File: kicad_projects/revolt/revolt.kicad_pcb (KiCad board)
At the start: 2 copper layers, 144.9 x 111.9 mm, 85 parts, among them J1 IDC-Header_2x07_P2.54mm_Verti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

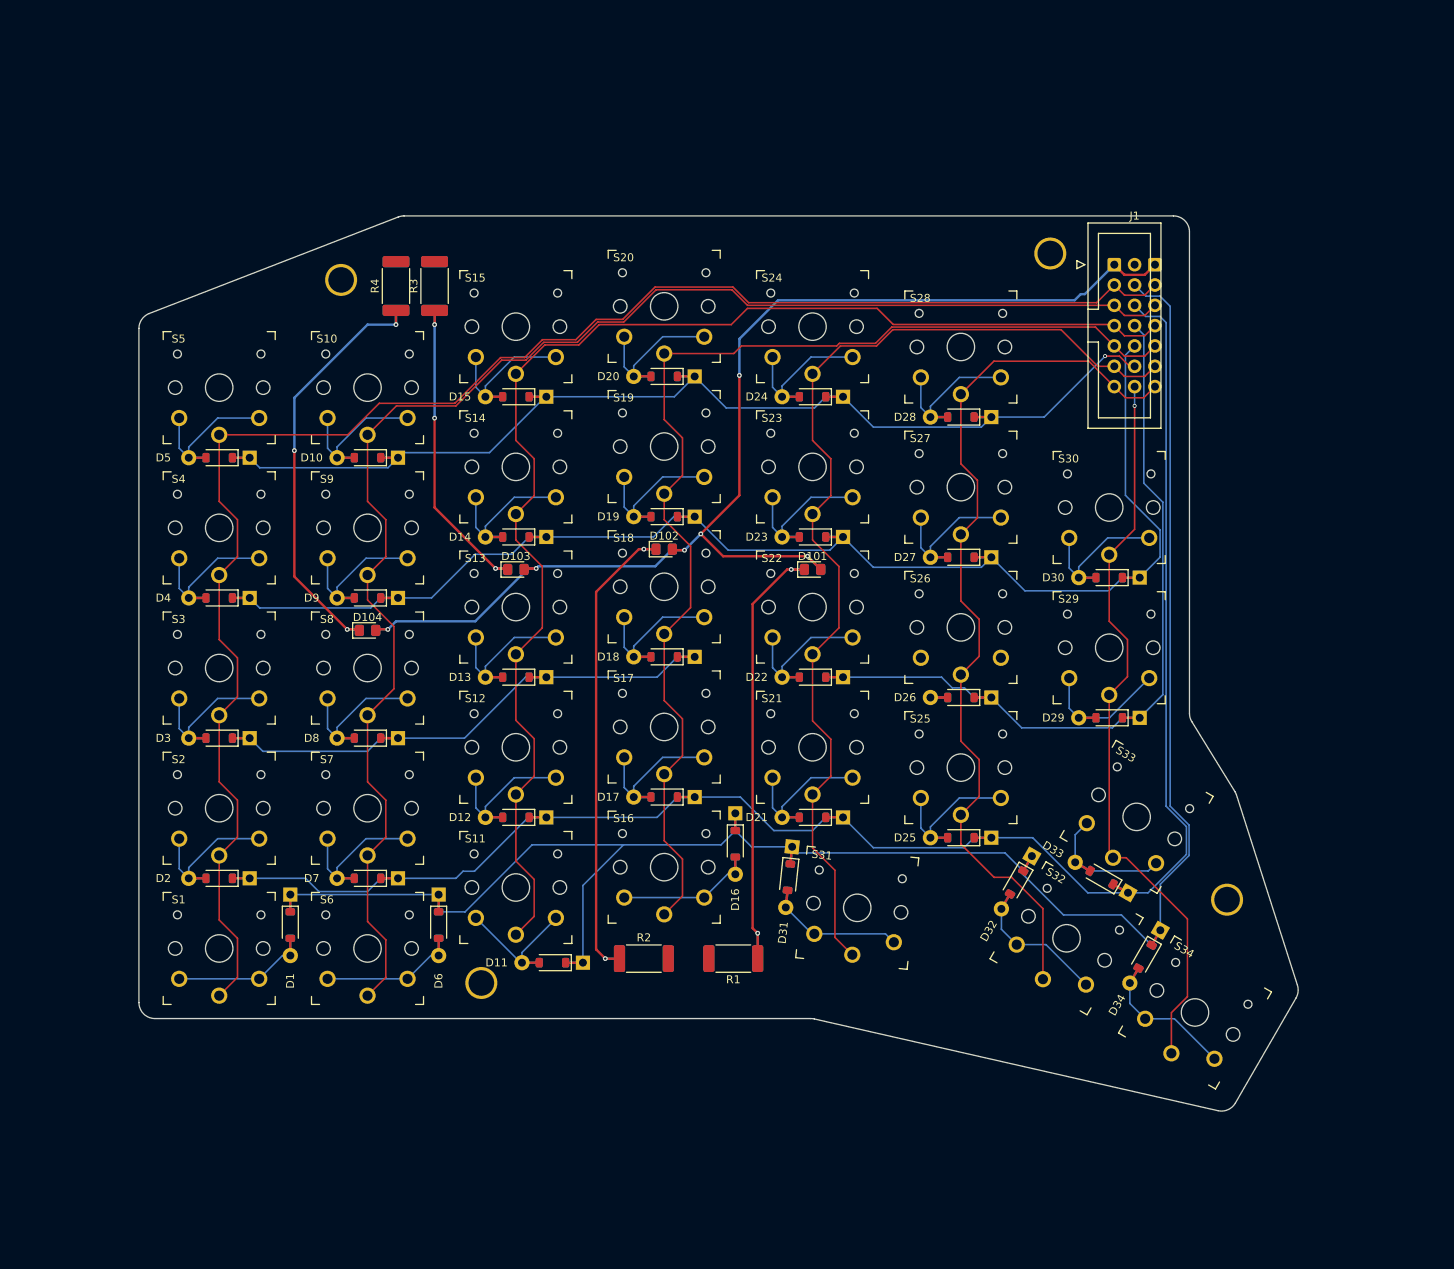
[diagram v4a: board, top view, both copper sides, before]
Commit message: Ground plane and stitching
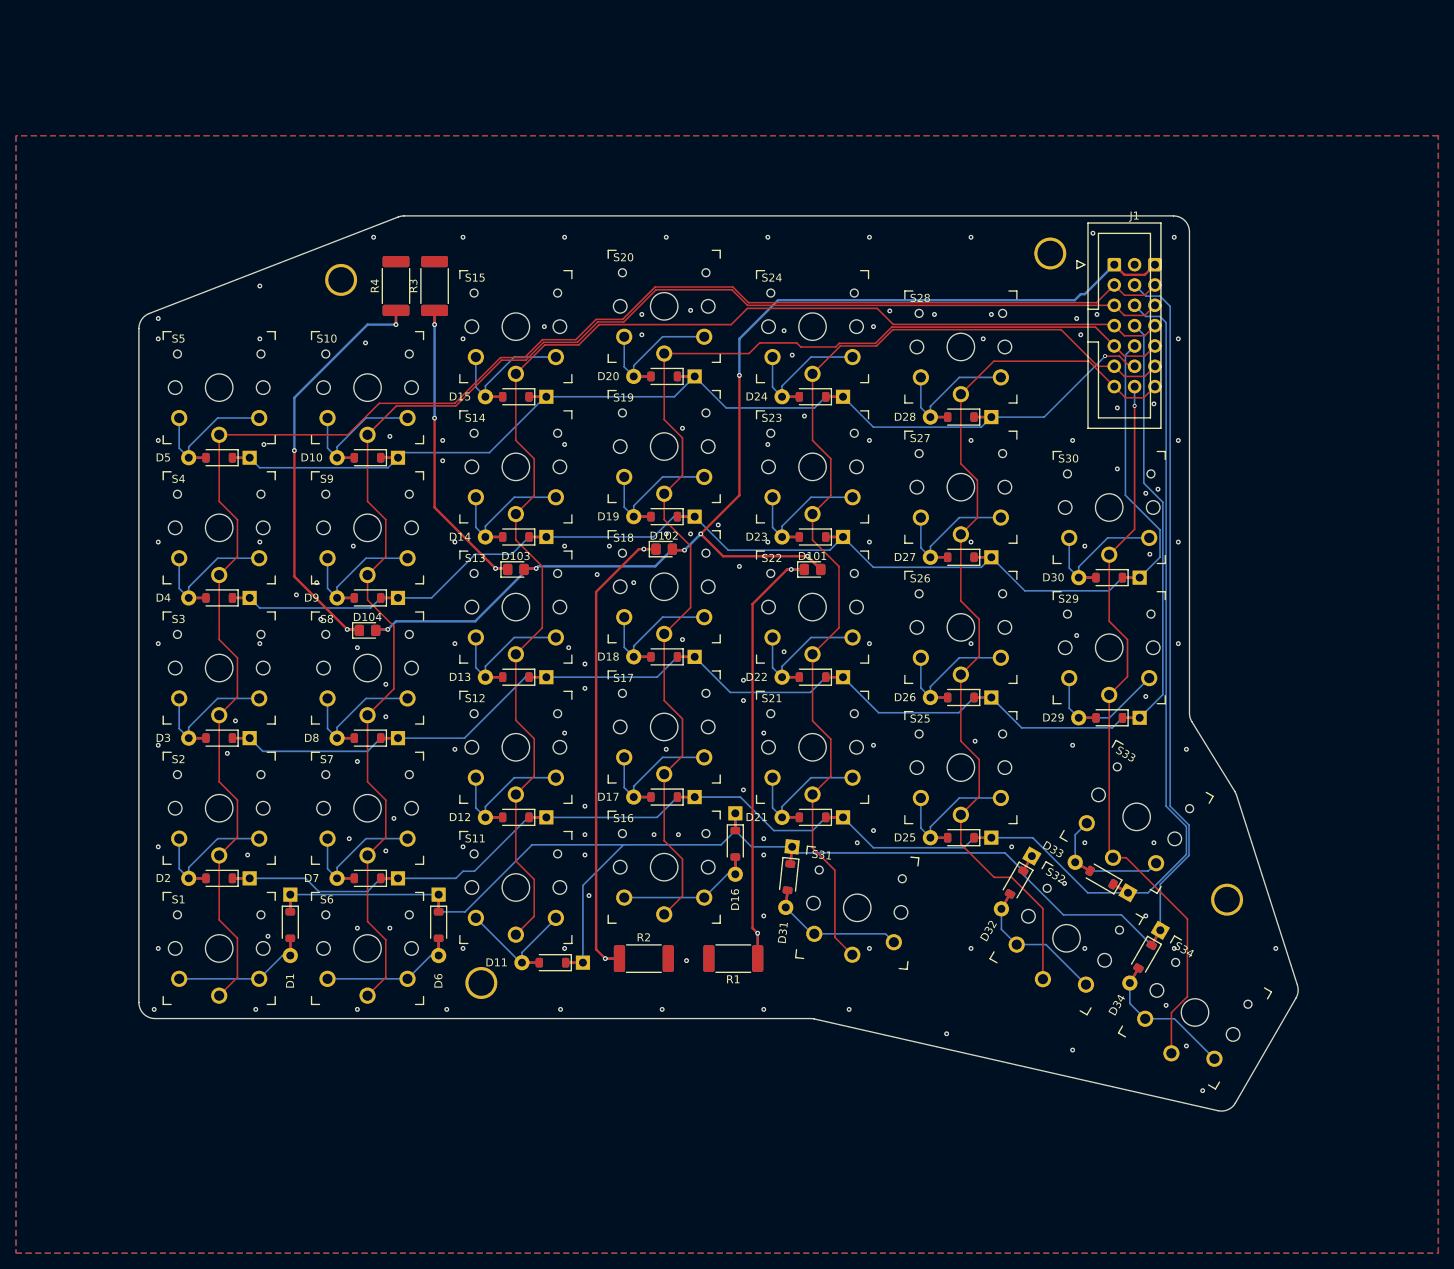
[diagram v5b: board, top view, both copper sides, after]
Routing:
- net /ROW2: track 142.3 -> 162.9 mm
- net Net-(D26-A): track 0.00 -> 17.1 mm
- net GND: vias 0 -> 147
- added copper zone on B.Cu, net GND
- added copper zone on F.Cu, net GND

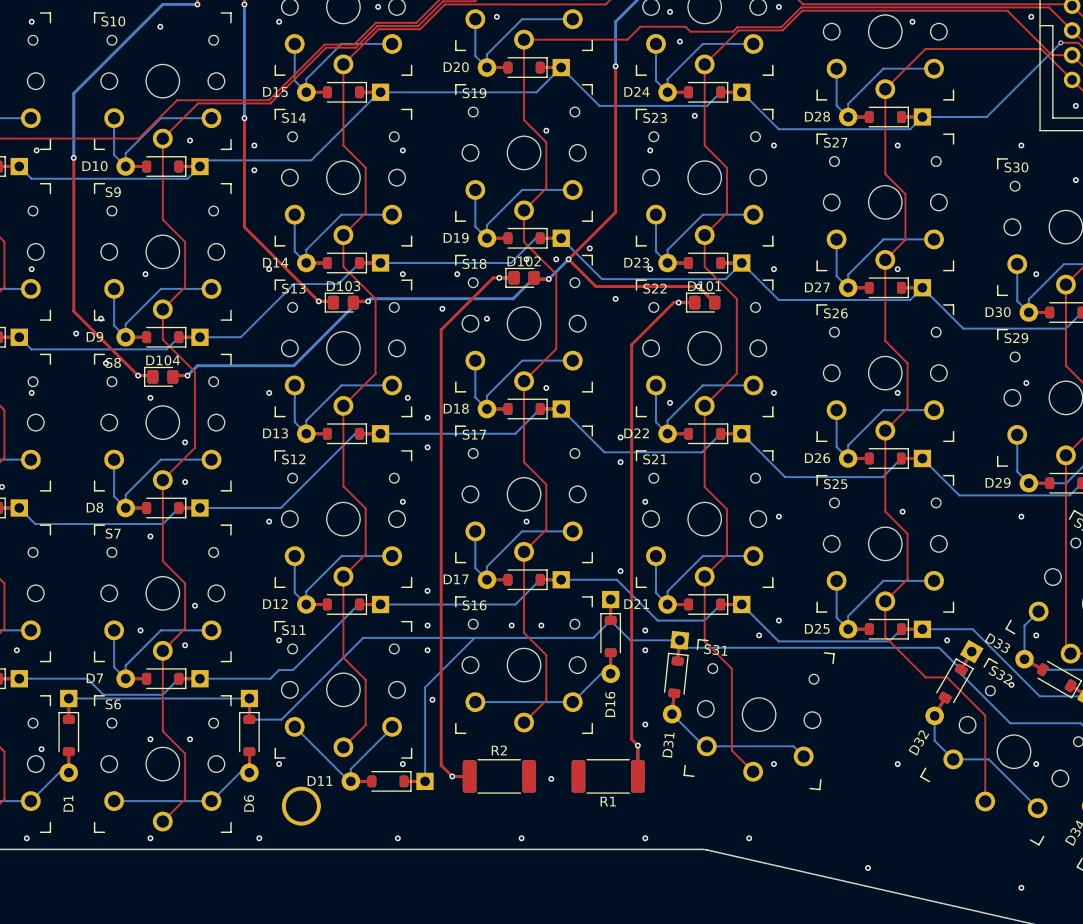
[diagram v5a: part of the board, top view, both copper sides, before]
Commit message: Add the url on the silkscreen, more stitching
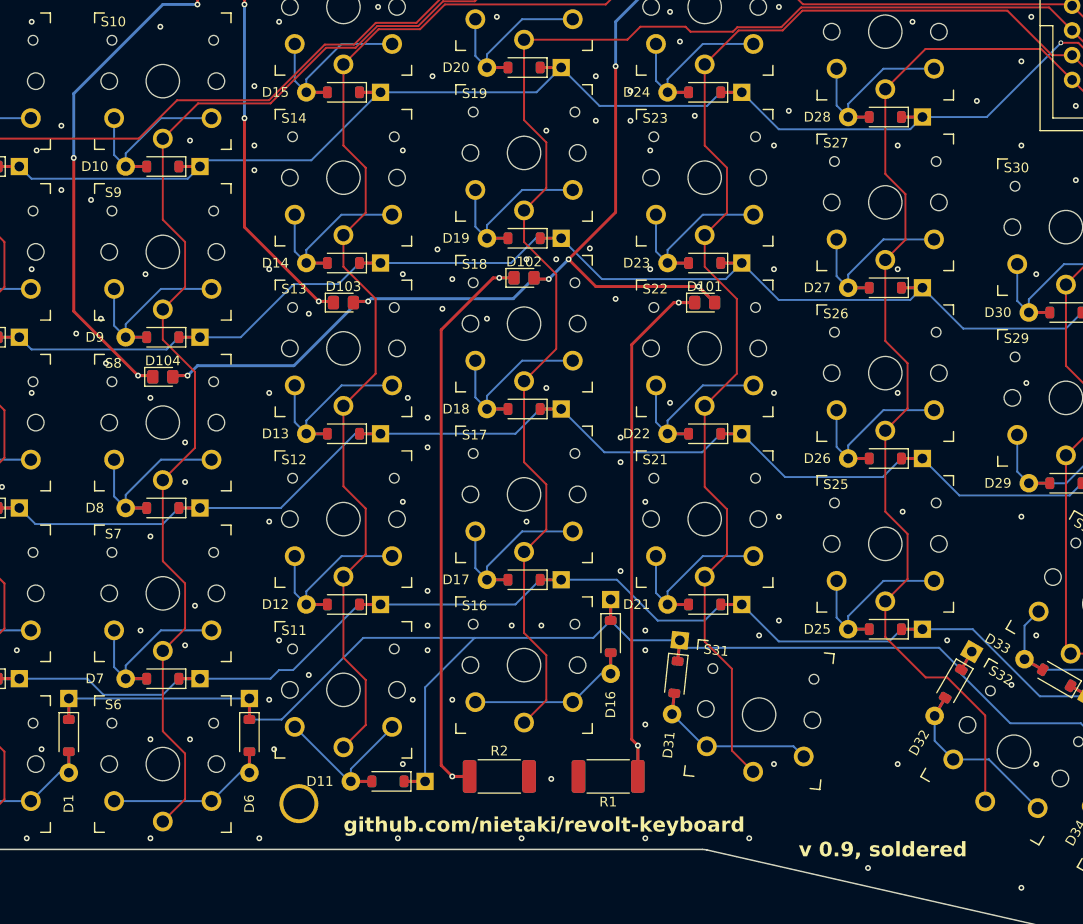
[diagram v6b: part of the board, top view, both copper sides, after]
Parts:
- moved H4 0.36 mm to (134.1, 156.5)
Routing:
- net GND: vias 147 -> 164
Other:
- board text added: "github.com/nietaki/revolt-keyboard"
- board text added: "v 0.9, soldered"
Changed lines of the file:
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@@
   )
   (footprint "revolt_footprints:HOLE_M3" (layer "F.Cu")
-    (at 134.366 156.718)
+    (at 134.112 156.464)
     (property "Sheetfile" "revolt.kicad_sch")
     (property "Sheetname" "")
@@
   (gr_line (start 228.765614 133.230142) (end 236.376007 156.985216)
     (stroke (width 0.15) (type solid)) (layer "Edge.Cuts"))
+  (gr_text "v 0.9, soldered" (at 185.42 162.052) (layer "F.SilkS")
+    (effects (font (size 1.5 1.5) (thickness 0.3) bold) (justify left bottom))
+  )
+  (gr_text "github.com/nietaki/revolt-keyboard" (at 138.684 159.512) (layer "F.SilkS")
+    (effects (font (size 1.5 1.5) (thickness 0.3) bold) (justify left bottom))
+  )
   (segment (start 220.472 72.136) (end 220.472 134.62) (width 0.2) (layer "B.Cu") (net 1))
   (segment (start 216.027 69.469) (end 217.417 70.859) (width 0.2) (layer "B.Cu") (net 1))
@@
   (via (at 93.98 76.2) (size 0.6) (drill 0.3) (layers "F.Cu" "B.Cu") (free) (net 48))
   (via (at 107.696 150.876) (size 0.6) (drill 0.3) (layers "F.Cu" "B.Cu") (free) (net 48))
-  (via (at 147.828 145.796) (size 0.6) (drill 0.3) (layers "F.Cu" "B.Cu") (free) (net 48))
+  (via (at 145.796 145.796) (size 0.6) (drill 0.3) (layers "F.Cu" "B.Cu") (free) (net 48))
   (via (at 103.632 123.952) (size 0.6) (drill 0.3) (layers "F.Cu" "B.Cu") (free) (net 48))
   (via (at 93.98 114.3) (size 0.6) (drill 0.3) (layers "F.Cu" "B.Cu") (free) (net 48))
   (via (at 221.488 114.3) (size 0.6) (drill 0.3) (layers "F.Cu" "B.Cu") (free) (net 48))
   (via (at 118.364 102.108) (size 0.6) (drill 0.3) (layers "F.Cu" "B.Cu") (free) (net 48))
+  (via (at 109.728 93.472) (size 0.6) (drill 0.3) (layers "F.Cu" "B.Cu") (free) (net 48))
   (via (at 183.388 74.676) (size 0.6) (drill 0.3) (layers "F.Cu" "B.Cu") (free) (net 48))
   (via (at 129.54 88.9) (size 0.6) (drill 0.3) (layers "F.Cu" "B.Cu") (free) (net 48))
@@
   (via (at 182.88 114.3) (size 0.6) (drill 0.3) (layers "F.Cu" "B.Cu") (free) (net 48))
   (via (at 220.98 63.5) (size 0.6) (drill 0.3) (layers "F.Cu" "B.Cu") (free) (net 48))
+  (via (at 203.708 84.328) (size 0.6) (drill 0.3) (layers "F.Cu" "B.Cu") (free) (net 48))
   (via (at 218.948 94.996) (size 0.6) (drill 0.3) (layers "F.Cu" "B.Cu") (free) (net 48))
   (via (at 207.264 144.272) (size 0.6) (drill 0.3) (layers "F.Cu" "B.Cu") (free) (net 48))
   (via (at 113.792 106.68) (size 0.6) (drill 0.3) (layers "F.Cu" "B.Cu") (free) (net 48))
-  (via (at 150.368 102.108) (size 0.6) (drill 0.3) (layers "F.Cu" "B.Cu") (free) (net 48))
+  (via (at 149.86 102.616) (size 0.6) (drill 0.3) (layers "F.Cu" "B.Cu") (free) (net 48))
   (via (at 118.872 160.02) (size 0.6) (drill 0.3) (layers "F.Cu" "B.Cu") (free) (net 48))
   (via (at 219.964 159.512) (size 0.6) (drill 0.3) (layers "F.Cu" "B.Cu") (free) (net 48))
+  (via (at 149.86 145.796) (size 0.6) (drill 0.3) (layers "F.Cu" "B.Cu") (free) (net 48))
   (via (at 154.432 73.152) (size 0.6) (drill 0.3) (layers "F.Cu" "B.Cu") (free) (net 48))
   (via (at 196.088 126.492) (size 0.6) (drill 0.3) (layers "F.Cu" "B.Cu") (free) (net 48))
@@
   (via (at 114.3 111.252) (size 0.6) (drill 0.3) (layers "F.Cu" "B.Cu") (free) (net 48))
   (via (at 169.672 160.02) (size 0.6) (drill 0.3) (layers "F.Cu" "B.Cu") (free) (net 48))
-  (via (at 132.08 152.4) (size 0.6) (drill 0.3) (layers "F.Cu" "B.Cu") (free) (net 48))
+  (via (at 131.572 150.876) (size 0.6) (drill 0.3) (layers "F.Cu" "B.Cu") (free) (net 48))
+  (via (at 164.592 81.788) (size 0.6) (drill 0.3) (layers "F.Cu" "B.Cu") (free) (net 48))
   (via (at 106.68 69.596) (size 0.6) (drill 0.3) (layers "F.Cu" "B.Cu") (free) (net 48))
+  (via (at 129.54 82.804) (size 0.6) (drill 0.3) (layers "F.Cu" "B.Cu") (free) (net 48))
   (via (at 172.212 75.184) (size 0.6) (drill 0.3) (layers "F.Cu" "B.Cu") (free) (net 48))
+  (via (at 184.404 85.344) (size 0.6) (drill 0.3) (layers "F.Cu" "B.Cu") (free) (net 48))
   (via (at 93.472 160.02) (size 0.6) (drill 0.3) (layers "F.Cu" "B.Cu") (free) (net 48))
+  (via (at 135.128 143.256) (size 0.6) (drill 0.3) (layers "F.Cu" "B.Cu") (free) (net 48))
   (via (at 131.064 101.6) (size 0.6) (drill 0.3) (layers "F.Cu" "B.Cu") (free) (net 48))
   (via (at 93.98 152.4) (size 0.6) (drill 0.3) (layers "F.Cu" "B.Cu") (free) (net 48))
@@
   (via (at 144.78 152.4) (size 0.6) (drill 0.3) (layers "F.Cu" "B.Cu") (free) (net 48))
   (via (at 157.48 63.5) (size 0.6) (drill 0.3) (layers "F.Cu" "B.Cu") (free) (net 48))
+  (via (at 148.336 99.568) (size 0.6) (drill 0.3) (layers "F.Cu" "B.Cu") (free) (net 48))
   (via (at 208.788 113.284) (size 0.6) (drill 0.3) (layers "F.Cu" "B.Cu") (free) (net 48))
+  (via (at 112.776 94.488) (size 0.6) (drill 0.3) (layers "F.Cu" "B.Cu") (free) (net 48))
   (via (at 153.416 106.68) (size 0.6) (drill 0.3) (layers "F.Cu" "B.Cu") (free) (net 48))
   (via (at 160.528 100.584) (size 0.6) (drill 0.3) (layers "F.Cu" "B.Cu") (free) (net 48))
@@
   (via (at 167.132 132.588) (size 0.6) (drill 0.3) (layers "F.Cu" "B.Cu") (free) (net 48))
   (via (at 208.788 73.66) (size 0.6) (drill 0.3) (layers "F.Cu" "B.Cu") (free) (net 48))
+  (via (at 135.128 106.172) (size 0.6) (drill 0.3) (layers "F.Cu" "B.Cu") (free) (net 48))
   (via (at 221.488 76.2) (size 0.6) (drill 0.3) (layers "F.Cu" "B.Cu") (free) (net 48))
   (via (at 122.936 88.392) (size 0.6) (drill 0.3) (layers "F.Cu" "B.Cu") (free) (net 48))
@@
   (via (at 208.28 165.1) (size 0.6) (drill 0.3) (layers "F.Cu" "B.Cu") (free) (net 48))
   (via (at 93.98 101.6) (size 0.6) (drill 0.3) (layers "F.Cu" "B.Cu") (free) (net 48))
+  (via (at 164.592 86.36) (size 0.6) (drill 0.3) (layers "F.Cu" "B.Cu") (free) (net 48))
   (via (at 182.88 152.4) (size 0.6) (drill 0.3) (layers "F.Cu" "B.Cu") (free) (net 48))
   (via (at 144.78 102.108) (size 0.6) (drill 0.3) (layers "F.Cu" "B.Cu") (free) (net 48))
@@
   (via (at 198.12 73.152) (size 0.6) (drill 0.3) (layers "F.Cu" "B.Cu") (free) (net 48))
   (via (at 195.58 88.9) (size 0.6) (drill 0.3) (layers "F.Cu" "B.Cu") (free) (net 48))
+  (via (at 131.064 145.796) (size 0.6) (drill 0.3) (layers "F.Cu" "B.Cu") (free) (net 48))
   (via (at 180.34 160.02) (size 0.6) (drill 0.3) (layers "F.Cu" "B.Cu") (free) (net 48))
   (via (at 118.872 149.86) (size 0.6) (drill 0.3) (layers "F.Cu" "B.Cu") (free) (net 48))
@@
   (via (at 191.008 73.152) (size 0.6) (drill 0.3) (layers "F.Cu" "B.Cu") (free) (net 48))
   (via (at 102.616 128.016) (size 0.6) (drill 0.3) (layers "F.Cu" "B.Cu") (free) (net 48))
+  (via (at 208.28 80.264) (size 0.6) (drill 0.3) (layers "F.Cu" "B.Cu") (free) (net 48))
   (via (at 173.228 78.232) (size 0.6) (drill 0.3) (layers "F.Cu" "B.Cu") (free) (net 48))
   (via (at 208.28 88.9) (size 0.6) (drill 0.3) (layers "F.Cu" "B.Cu") (free) (net 48))
@@
   (via (at 132.08 63.5) (size 0.6) (drill 0.3) (layers "F.Cu" "B.Cu") (free) (net 48))
   (via (at 130.048 160.02) (size 0.6) (drill 0.3) (layers "F.Cu" "B.Cu") (free) (net 48))
+  (via (at 168.148 86.36) (size 0.6) (drill 0.3) (layers "F.Cu" "B.Cu") (free) (net 48))
+  (via (at 147.828 81.788) (size 0.6) (drill 0.3) (layers "F.Cu" "B.Cu") (free) (net 48))
   (via (at 211.328 73.152) (size 0.6) (drill 0.3) (layers "F.Cu" "B.Cu") (free) (net 48))
   (via (at 93.98 88.9) (size 0.6) (drill 0.3) (layers "F.Cu" "B.Cu") (free) (net 48))
   (via (at 144.272 160.02) (size 0.6) (drill 0.3) (layers "F.Cu" "B.Cu") (free) (net 48))
+  (via (at 109.728 86.868) (size 0.6) (drill 0.3) (layers "F.Cu" "B.Cu") (free) (net 48))
   (via (at 154.432 75.692) (size 0.6) (drill 0.3) (layers "F.Cu" "B.Cu") (free) (net 48))
   (via (at 167.132 121.412) (size 0.6) (drill 0.3) (layers "F.Cu" "B.Cu") (free) (net 48))
   (via (at 117.856 138.684) (size 0.6) (drill 0.3) (layers "F.Cu" "B.Cu") (free) (net 48))
   (via (at 182.88 63.5) (size 0.6) (drill 0.3) (layers "F.Cu" "B.Cu") (free) (net 48))
+  (via (at 168.148 83.312) (size 0.6) (drill 0.3) (layers "F.Cu" "B.Cu") (free) (net 48))
   (via (at 106.68 101.6) (size 0.6) (drill 0.3) (layers "F.Cu" "B.Cu") (free) (net 48))
   (via (at 159.512 113.792) (size 0.6) (drill 0.3) (layers "F.Cu" "B.Cu") (free) (net 48))

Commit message: Cosmetic changes
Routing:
- net Net-(D33-A): track 14.1 -> 17.3 mm
- net V5V: track 153.0 -> 154.3 mm
- net Net-(D10-A): track 17.1 -> 17.9 mm
- net Net-(D104-K): track 54.9 -> 55.6 mm
- net /ROW3: track 193.6 -> 194.2 mm
- net /ROW2: track 162.9 -> 163.4 mm
- net GND: vias 164 -> 181
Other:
- board text added: "v0.9, soldered"
- board text removed: "v 0.9, soldered"

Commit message: Commander board
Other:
- rule pad_to_mask_clearance: 0.05 -> 0
